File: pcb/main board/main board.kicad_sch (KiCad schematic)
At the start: 35 parts, among them J1 Motor Conn 0, J2 Motor Conn 1, J3 Motor Conn 2, J4 Motor Conn 3, U1 L298HN, U2 L298HN, U3 LM2596S-5, U4 MCP23017_SO, U5 LMZ13608

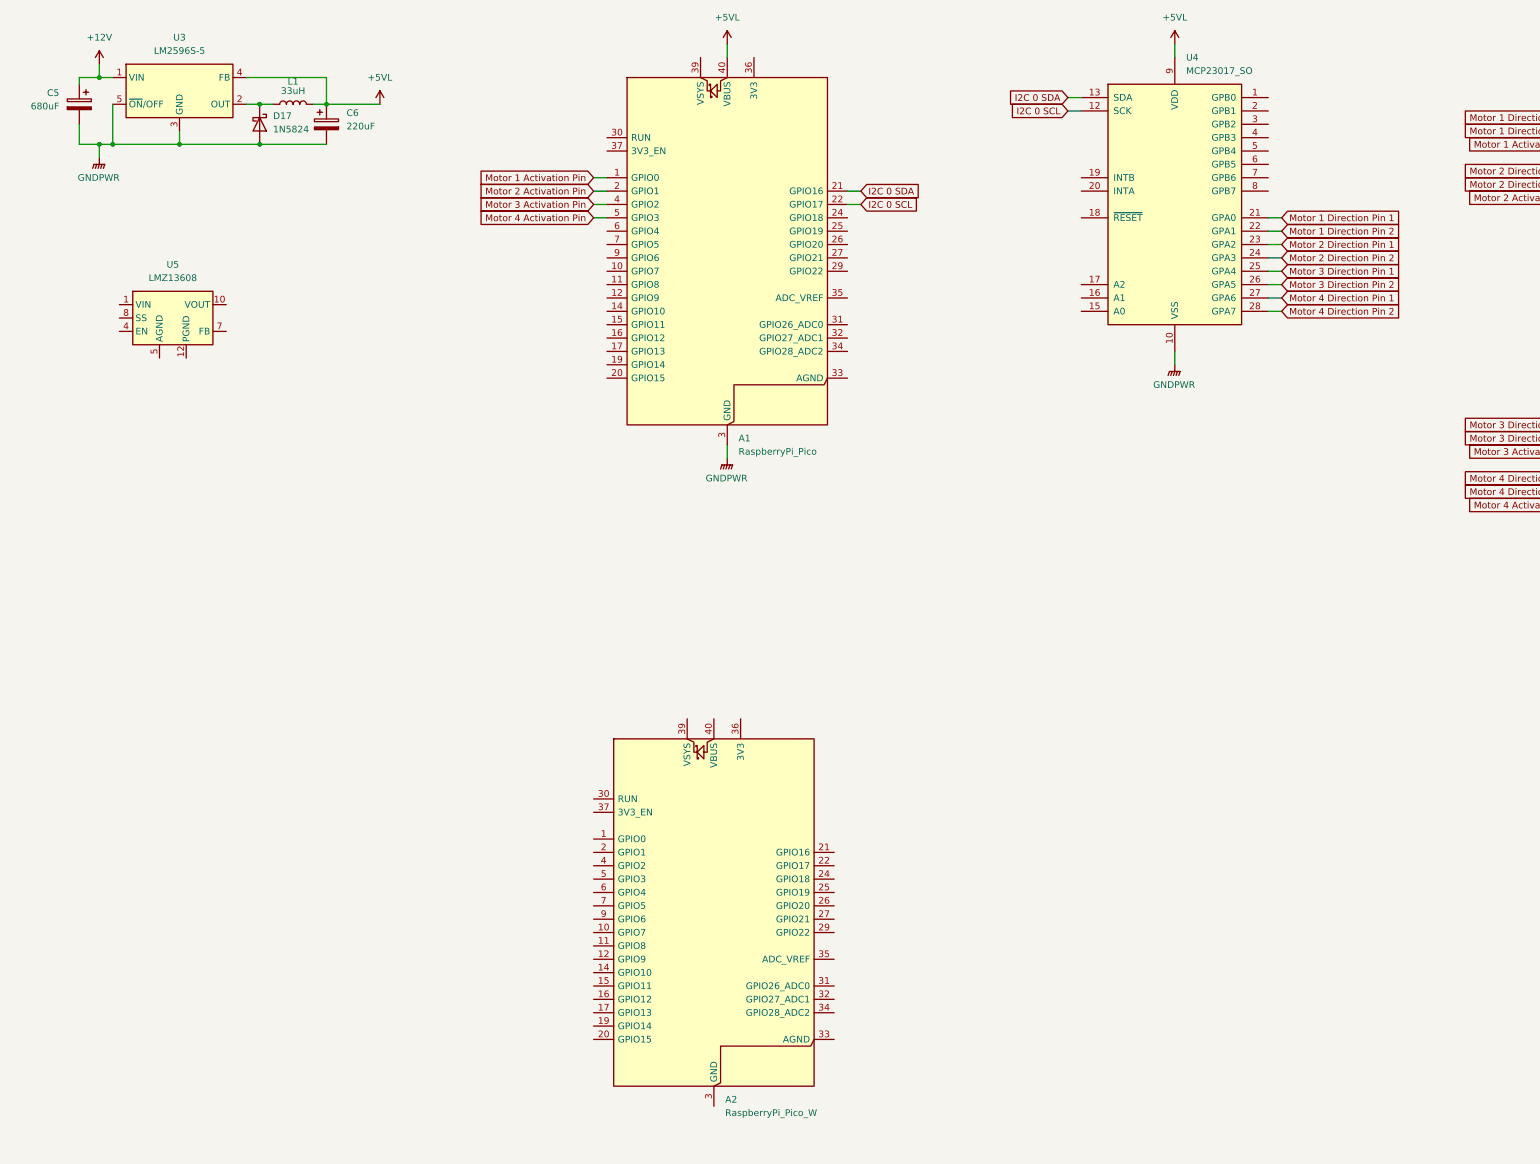
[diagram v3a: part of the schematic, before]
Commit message: Almost finished implementation of 5v power regulator
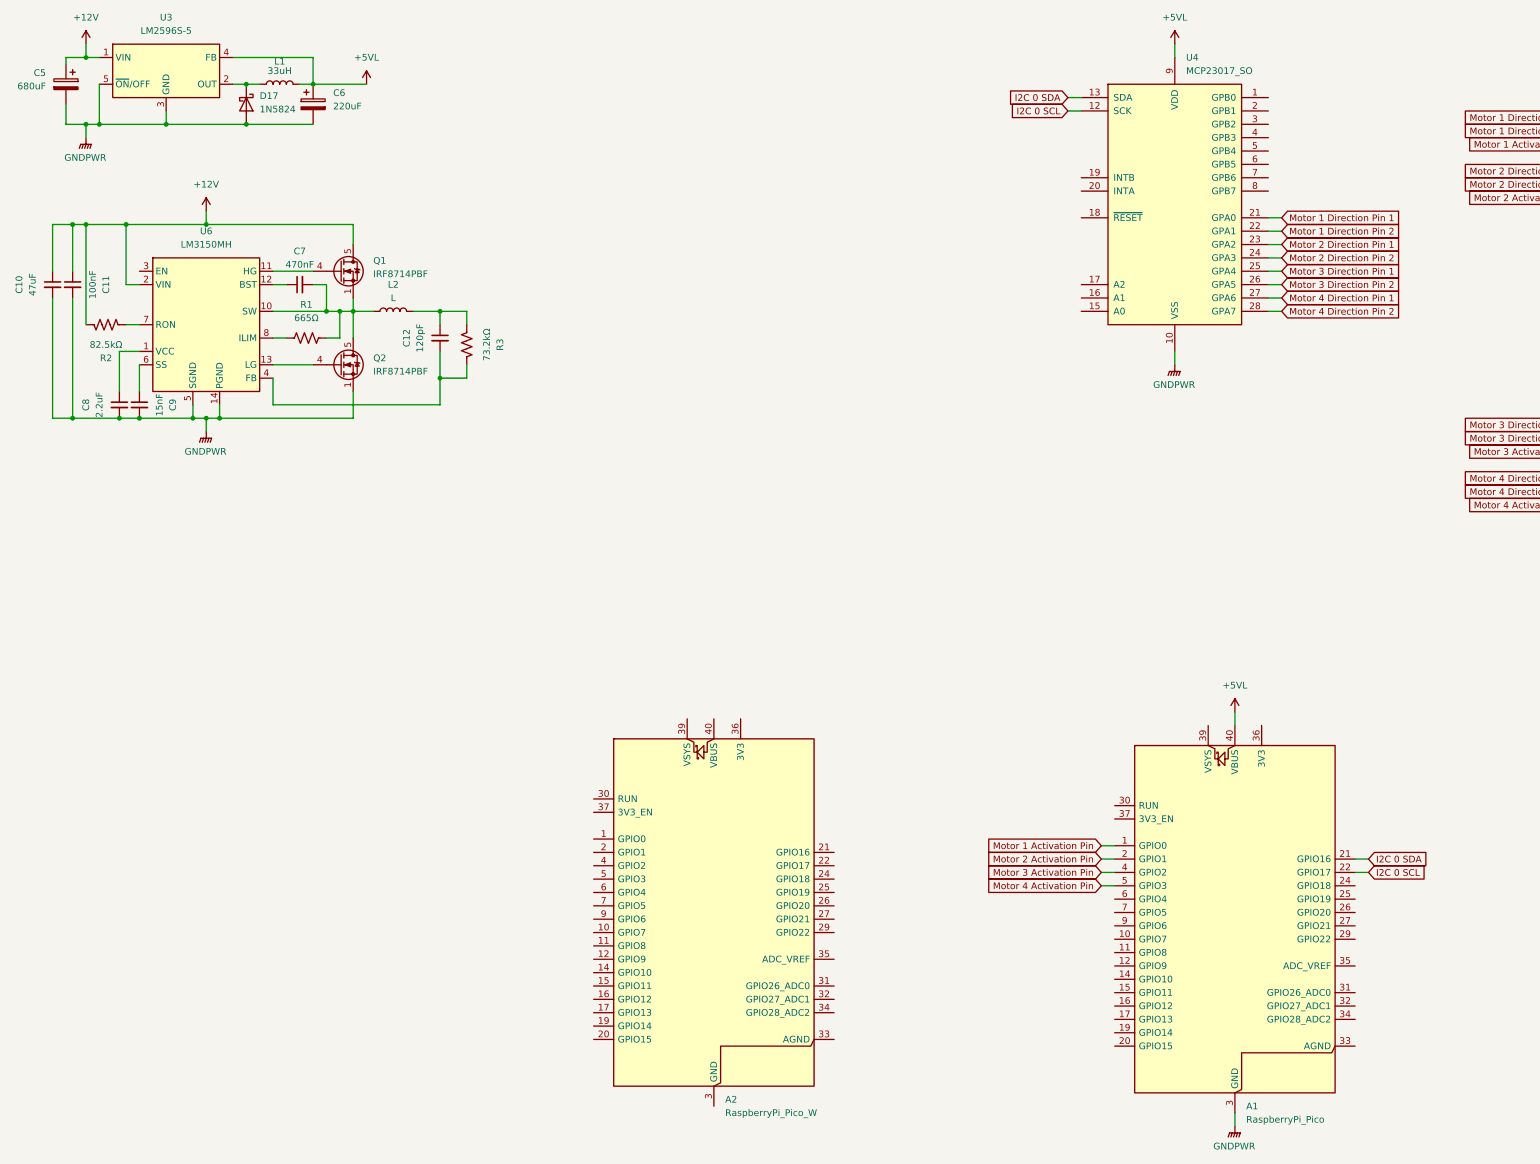
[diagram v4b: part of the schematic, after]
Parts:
- removed U5: LMZ13608, Package_TO_SOT_SMD:Texas_NDY0011A, symbol Regulator_Switching:LMZ13608
- added C10: 47uF, symbol Device:C_Small
- added C11: 100nF, symbol Device:C_Small
- added C12: 120pF, symbol Device:C_Small
- added C7: 470nF, symbol Device:C_Small
- added C8: 2.2uF, symbol Device:C_Small
- added C9: 15nF, symbol Device:C_Small
- added L2: L, symbol Device:L
- added Q1, Q2: IRF8714PBF, Package_SO:SOIC-8_3.9x4.9mm_P1.27mm, symbol Transistor_FET:IRF8721PBF-1
- added R1: 665Ω, symbol Device:R_US
- added R2: 82.5kΩ, symbol Device:R_US
- added R3: 73.2kΩ, symbol Device:R_US
- added U6: LM3150MH, Package_SO:HTSSOP-14-1EP_4.4x5mm_P0.65mm_EP3.4x5mm_Mask3x3.1mm, symbol Regulator_Switching:LM3150MH
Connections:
- net +12V: now also C10.1, C11.1, Q1.5 (D), Q1.6 (D), Q1.7 (D), Q1.8 (D), R2.1, U6.2 (VIN)
- net GNDPWR: now also C10.2, C11.2, C8.2, C9.2, Q2.1 (S), Q2.2 (S), Q2.3 (S), U6.14 (PGND), U6.15 (SGND), U6.5 (SGND), U6.9 (SGND)
- new net: Q2.4 (G), U6.13 (LG)
- new net: C7.2, L2.1, Q1.1 (S), Q1.2 (S), Q1.3 (S), Q2.5 (D), Q2.6 (D), Q2.7 (D), Q2.8 (D), R1.2, U6.10 (SW)
- new net: C8.1, U6.1 (VCC)
- new net: Q1.4 (G), U6.11 (HG)
- new net: C7.1, U6.12 (BST)
- new net: C12.2, R3.1, U6.4 (FB)
- new net: C9.1, U6.6 (SS)
- new net: R2.2, U6.7 (RON)
- new net: R1.1, U6.8 (ILIM)
- new net: C12.1, L2.2, R3.2
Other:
- moved on the sheet: A1, C5, C6, D17, L1, U3

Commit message: Finished 5V power alimentation and mcp23017 connection
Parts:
- removed C5: 680uF, symbol Device:C_Polarized
- removed C6: 220uF, symbol Device:C_Polarized
- added C13: 120uF, symbol Device:C_Polarized_Small_US
- added C5: 680uF, symbol Device:C_Polarized_Small_US
- added C6: 220uF, symbol Device:C_Polarized_Small_US
- added J5: I2C 0 Conn, symbol Connector_Generic:Conn_01x04
- added J6: I2C 1 Conn, symbol Connector_Generic:Conn_01x04
- added R4: 10kΩ, symbol Device:R_US
- J1: value Motor Conn 0 -> Motor 0 Conn
- J2: value Motor Conn 1 -> Motor 1 Conn
- J3: value Motor Conn 2 -> Motor 2 Conn
- J4: value Motor Conn 3 -> Motor 3 Conn
- L2: value L -> 1.8uH
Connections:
- net +12V: now also C5.1
- net +5VL: now also U4.18 (~{RESET}), C6.1
- net GNDPWR: now also U4.15 (A0), U4.16 (A1), U4.17 (A2), C5.2, C6.2, J5.4 (Pin_4), J6.4 (Pin_4)
- net I2C 0 SCL: now also J5.3 (Pin_3)
- net I2C 0 SDA: now also J5.2 (Pin_2)
- net at C12.2, R3.1, U6.4 (FB): now also R4.1
- net +5VP: now reaches C12.1, L2.2, R3.2
- net +5VP: now also C13.1, J5.1 (Pin_1), J6.1 (Pin_1)
- new net: C13.2, R4.2
- new net I2C 1 SCL: J6.3 (Pin_3)
- new net I2C 1 SDA: J6.2 (Pin_2)
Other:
- moved on the sheet: A1, A2, C10, C11, C12, C7, C8, C9, L2, Q1, Q2, R1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

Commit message: Started to implement steppers motors drivers
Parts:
- added A3: Pololu_Breakout_A4988, Module:Pololu_Breakout-16_15.2x20.3mm, symbol Driver_Motor:Pololu_Breakout_A4988
- added J7: Stepper 0 Conn, symbol Connector_Generic:Conn_01x04
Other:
- moved on the sheet: J5, J6

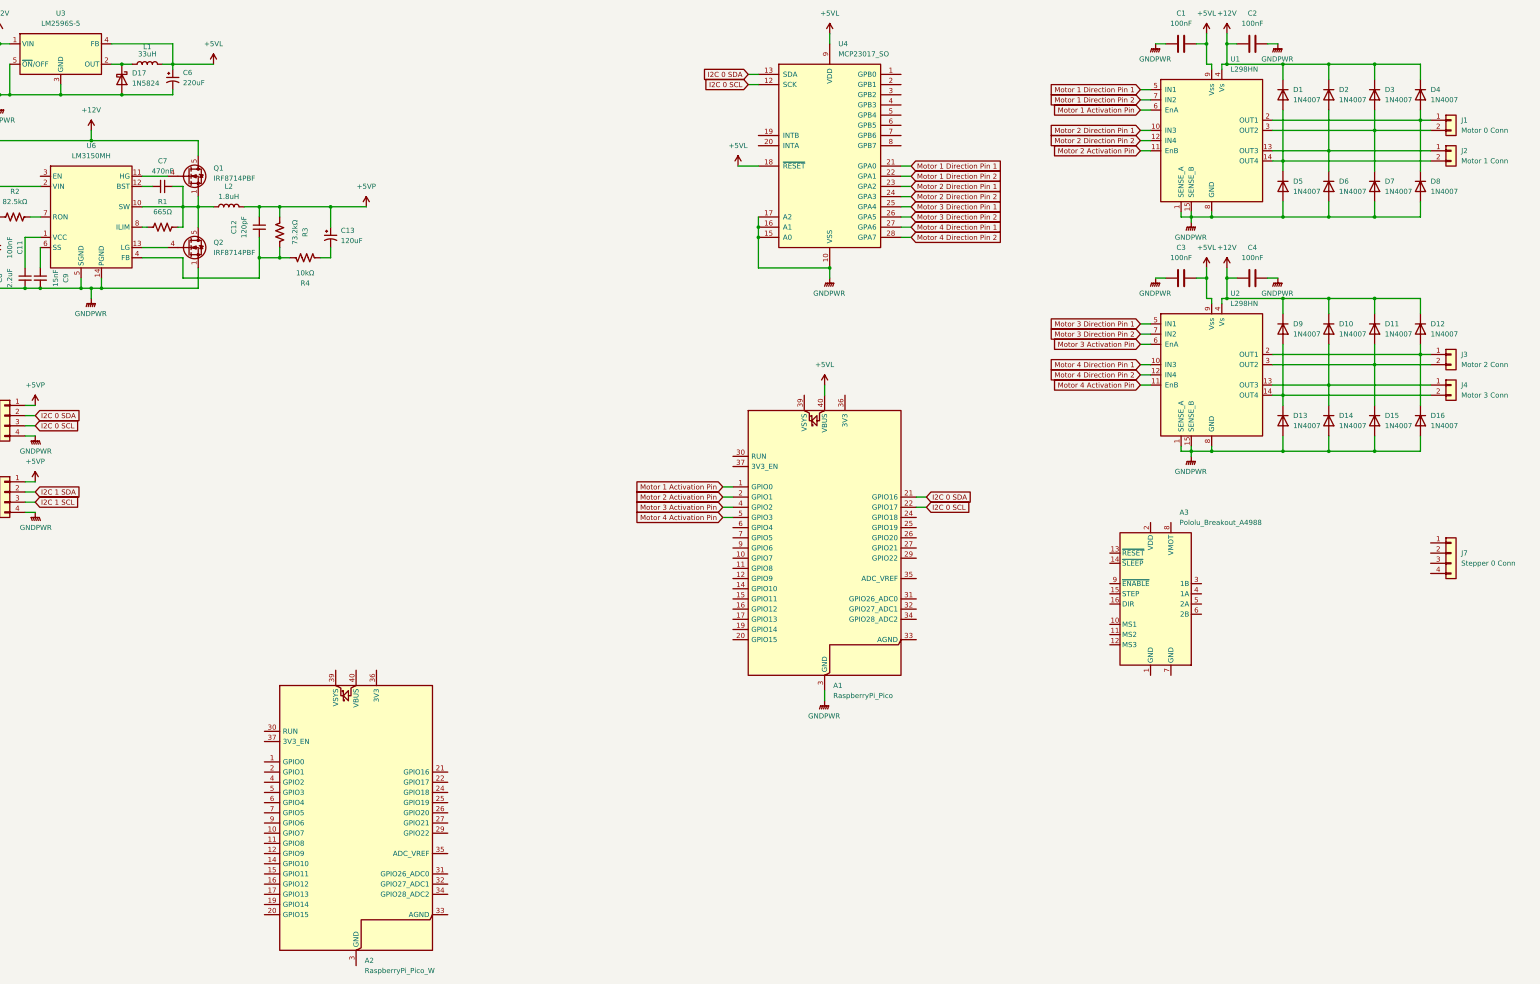
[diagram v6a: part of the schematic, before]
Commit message: Finished to implement and connect every 3 steppers drivers
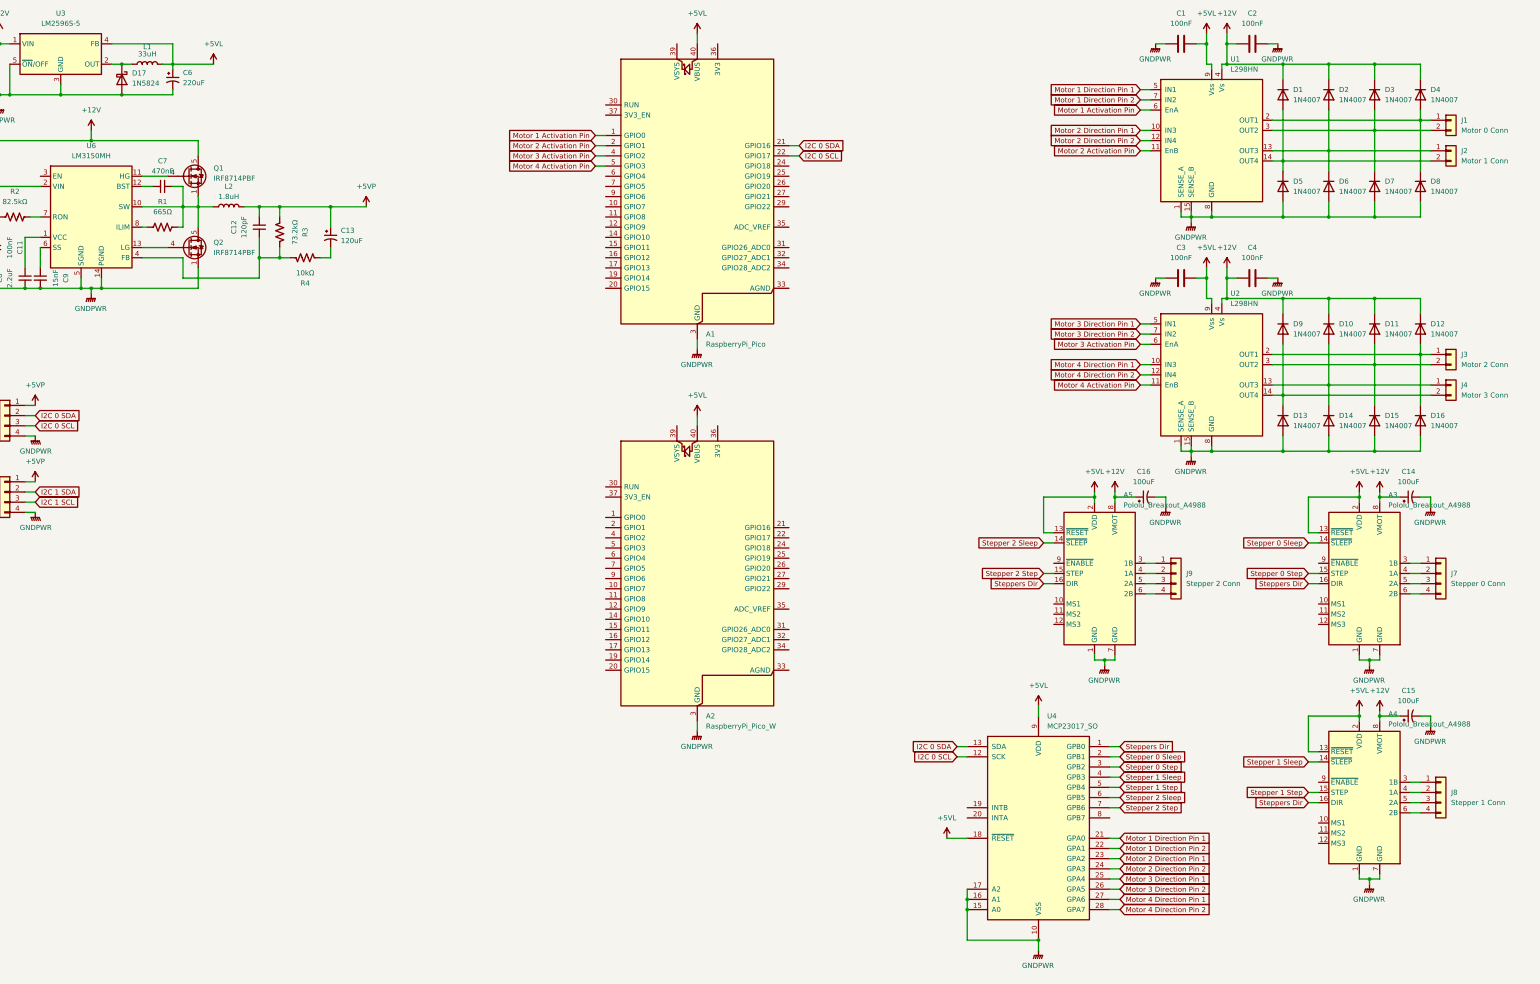
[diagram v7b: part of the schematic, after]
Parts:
- added A4, A5: Pololu_Breakout_A4988, Module:Pololu_Breakout-16_15.2x20.3mm, symbol Driver_Motor:Pololu_Breakout_A4988
- added C14, C15, C16: 100uF, symbol Device:C_Polarized_Small_US
- added J8: Stepper 1 Conn, symbol Connector_Generic:Conn_01x04
- added J9: Stepper 2 Conn, symbol Connector_Generic:Conn_01x04
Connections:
- net +12V: now also A3.8 (VMOT), A4.8 (VMOT), A5.8 (VMOT), C14.1, C15.1, C16.1
- net +5VL: now also A2.40 (VBUS), A3.13 (~{RESET}), A3.2 (VDD), A4.13 (~{RESET}), A4.2 (VDD), A5.13 (~{RESET}), A5.2 (VDD)
- net GNDPWR: now also A2.13 (GND), A2.18 (GND), A2.23 (GND), A2.28 (GND), A2.3 (GND), A2.38 (GND), A2.8 (GND), A3.1 (GND), A3.7 (GND), A4.1 (GND), A4.7 (GND), A5.1 (GND), A5.7 (GND), C14.2, C15.2, C16.2
- net at J7.1 (Pin_1): now also A3.3 (1B)
- net at J7.2 (Pin_2): now also A3.4 (1A)
- net at J7.3 (Pin_3): now also A3.5 (2A)
- net at J7.4 (Pin_4): now also A3.6 (2B)
- net Steppers Dir: now reaches U4.1 (GPB0)
- net Steppers Dir: now also A3.16 (DIR), A4.16 (DIR), A5.16 (DIR)
- net Stepper 0 Sleep: now reaches U4.2 (GPB1)
- net Stepper 0 Sleep: now also A3.14 (~{SLEEP})
- net Stepper 0 Step: now reaches U4.3 (GPB2)
- net Stepper 0 Step: now also A3.15 (STEP)
- net Stepper 1 Sleep: now reaches U4.4 (GPB3)
- net Stepper 1 Sleep: now also A4.14 (~{SLEEP})
- net Stepper 1 Step: now reaches U4.5 (GPB4)
- net Stepper 1 Step: now also A4.15 (STEP)
- net Stepper 2 Sleep: now reaches U4.6 (GPB5)
- net Stepper 2 Sleep: now also A5.14 (~{SLEEP})
- net Stepper 2 Step: now reaches U4.7 (GPB6)
- net Stepper 2 Step: now also A5.15 (STEP)
- new net: A5.3 (1B), J9.1 (Pin_1)
- new net: A5.4 (1A), J9.2 (Pin_2)
- new net: A5.5 (2A), J9.3 (Pin_3)
- new net: A5.6 (2B), J9.4 (Pin_4)
- new net: A4.3 (1B), J8.1 (Pin_1)
- new net: A4.4 (1A), J8.2 (Pin_2)
- new net: A4.5 (2A), J8.3 (Pin_3)
- new net: A4.6 (2B), J8.4 (Pin_4)
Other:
- moved on the sheet: A1, A2, A3, J7, U4

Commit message: Theroricaly finished main board !
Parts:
- removed A3, A4, A5: Pololu_Breakout_A4988, Module:Pololu_Breakout-16_15.2x20.3mm, symbol Driver_Motor:Pololu_Breakout_A4988
- removed C1, C2, C3, C4: 100nF, symbol Device:C
- removed C14, C15, C16: 100uF, symbol Device:C_Polarized_Small_US
- removed D1, D10, D11, D12, D13, D14, D15, D16, D2, D3, D4, D5, D6, D7, D8, D9: 1N4007, Diode_THT:D_DO-41_SOD81_P10.16mm_Horizontal, symbol Diode:1N4007
- removed J1: Motor 0 Conn, symbol Connector_Generic:Conn_01x02
- removed J2: Motor 1 Conn, symbol Connector_Generic:Conn_01x02
- removed J3: Motor 2 Conn, symbol Connector_Generic:Conn_01x02
- removed J4: Motor 3 Conn, symbol Connector_Generic:Conn_01x02
- removed J7: Stepper 0 Conn, symbol Connector_Generic:Conn_01x04
- removed J8: Stepper 1 Conn, symbol Connector_Generic:Conn_01x04
- removed J9: Stepper 2 Conn, symbol Connector_Generic:Conn_01x04
- removed U1, U2: L298HN, Package_TO_SOT_THT:TO-220-15_P2.54x2.54mm_StaggerOdd_Lead5.84mm_TabDown, symbol Driver_Motor:L298HN
- added J10: 12V Battery, symbol Connector_Generic:Conn_01x02
- added J11: BAU, symbol Connector_Generic:Conn_01x02
- added J12: Servo 4 Conn, symbol Connector_Generic:Conn_01x03
- added J13: Servo 1 Conn, symbol Connector_Generic:Conn_01x03
- added J14: Servo 2 Conn, symbol Connector_Generic:Conn_01x03
- added J15: Servo 3 Conn, symbol Connector_Generic:Conn_01x03
- added J16: Servo 5 Conn, symbol Connector_Generic:Conn_01x03
- added J17: Servo 6 Conn, symbol Connector_Generic:Conn_01x03
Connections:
- net +12V: now also J10.1 (Pin_1)
- net +5VP: now also J12.1 (Pin_1), J13.1 (Pin_1), J14.1 (Pin_1), J15.1 (Pin_1), J16.1 (Pin_1), J17.1 (Pin_1)
- net GNDPWR: now also J11.2 (Pin_2), J12.2 (Pin_2), J13.2 (Pin_2), J14.2 (Pin_2), J15.2 (Pin_2), J16.2 (Pin_2), J17.2 (Pin_2)
- net I2C 0 SCL: now also A2.22 (GPIO17)
- net I2C 0 SDA: now also A2.21 (GPIO16)
- net I2C 1 SCL: now also A2.25 (GPIO19)
- net I2C 1 SDA: now also A2.24 (GPIO18)
- net Motor 1 Direction Pin 1: now also U4.1 (GPB0); no longer U4.21 (GPA0)
- net Motor 1 Direction Pin 2: now also U4.2 (GPB1); no longer U4.22 (GPA1)
- net Motor 2 Direction Pin 1: now also U4.3 (GPB2); no longer U4.23 (GPA2)
- net Motor 2 Direction Pin 2: now also U4.4 (GPB3); no longer U4.24 (GPA3)
- net Motor 3 Direction Pin 1: now also U4.5 (GPB4); no longer U4.25 (GPA4)
- net Motor 3 Direction Pin 2: now also U4.6 (GPB5); no longer U4.26 (GPA5)
- net Motor 4 Direction Pin 1: now also U4.7 (GPB6); no longer U4.27 (GPA6)
- net Motor 4 Direction Pin 2: now also U4.8 (GPB7); no longer U4.28 (GPA7)
- net Stepper 0 Sleep: now also U4.22 (GPA1); no longer U4.2 (GPB1)
- net Stepper 0 Step: now also U4.23 (GPA2); no longer U4.3 (GPB2)
- net Stepper 1 Sleep: now also U4.24 (GPA3); no longer U4.4 (GPB3)
- net Stepper 1 Step: now also U4.25 (GPA4); no longer U4.5 (GPB4)
- net Stepper 2 Sleep: now also U4.26 (GPA5); no longer U4.6 (GPB5)
- net Stepper 2 Step: now also U4.27 (GPA6); no longer U4.7 (GPB6)
- net Steppers Dir: now also U4.21 (GPA0); no longer U4.1 (GPB0)
- net Servo 4 PWM: now reaches A1.10 (GPIO7)
- net Servo 4 PWM: now also J12.3 (Pin_3)
- net Servo 5 PWM: now reaches A1.11 (GPIO8)
- net Servo 5 PWM: now also J16.3 (Pin_3)
- net Servo 6 PWM: now reaches A1.12 (GPIO9)
- net Servo 6 PWM: now also J17.3 (Pin_3)
- net Servo 1 PWM: now reaches A1.6 (GPIO4)
- net Servo 1 PWM: now also J13.3 (Pin_3)
- net Servo 2 PWM: now reaches A1.7 (GPIO5)
- net Servo 2 PWM: now also J14.3 (Pin_3)
- net Servo 3 PWM: now reaches A1.9 (GPIO6)
- net Servo 3 PWM: now also J15.3 (Pin_3)
- new net: J10.2 (Pin_2), J11.1 (Pin_1)
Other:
- added sheet motors and steppers drivers (motors and steppers drivers.kicad_sch)
- moved on the sheet: A1, A2, U4
